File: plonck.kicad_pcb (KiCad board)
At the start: 2 copper layers, 228.6 x 76.2 mm, 127 parts, among them J1 Battery_connector, J2 SWD, J3 Reset, Q1 Q_PMOS_DSG, U1 SRV05-4, U2 TP4054-42-SOT25-R, U3 XC6206PxxxMR-Regulator_Linear, U4 nRF52840_holyiot_18010, q1 USB4085-GF-A_REVA

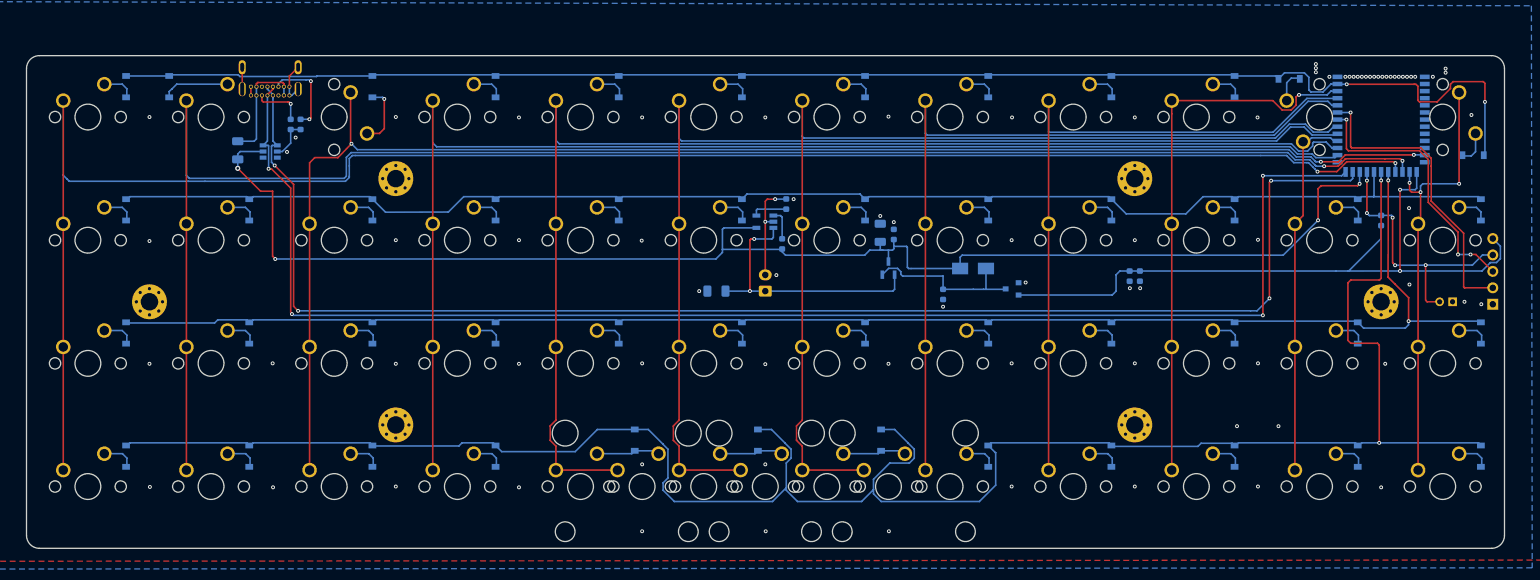
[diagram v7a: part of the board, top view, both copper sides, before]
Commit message: various fixes and additions
changed switch footprints to be alps compatible
added descriptive text to bottom row
fixed mounting holes not being connected to ground
fixed incorrectly wired esd chip
added reset switch in default planck position
changed mx3 to normal rotation
changed board outline to move usb port further out
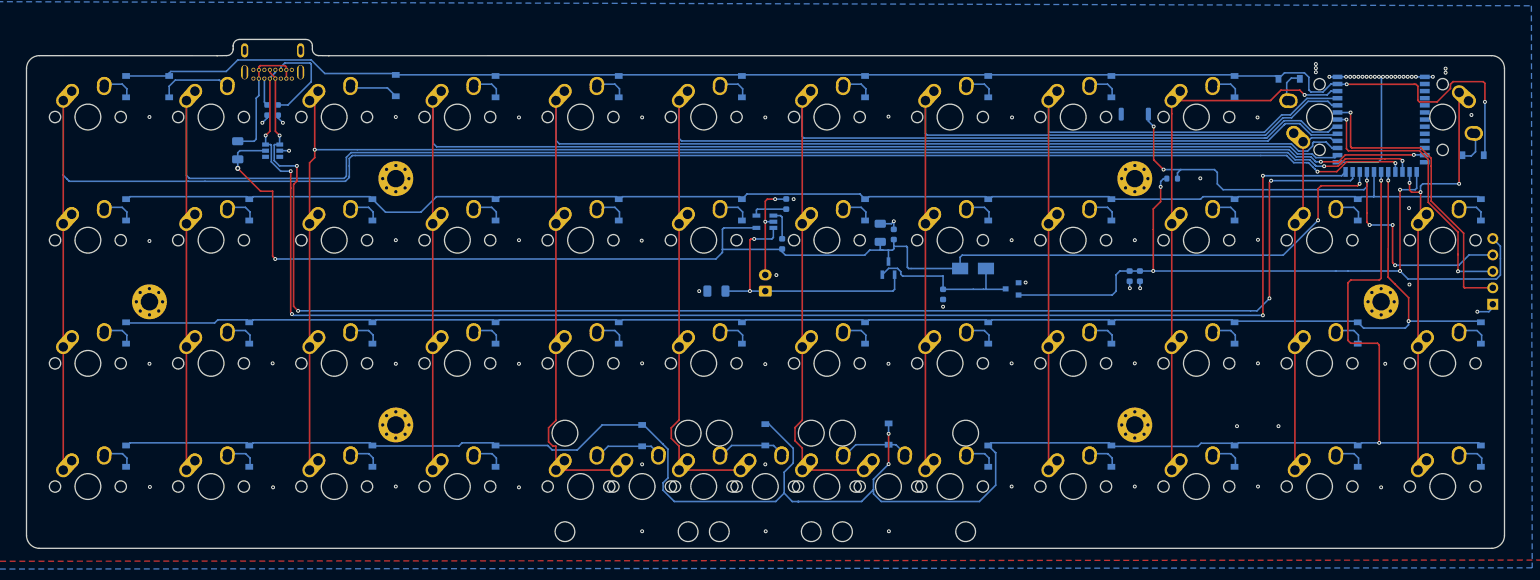
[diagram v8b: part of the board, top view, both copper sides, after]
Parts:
- removed J3: Reset, Connector_PinHeader_2.00mm:PinHeader_1x02_P2.00mm_Vertical
- added SW1: SW_Push, Button_Switch_SMD:SW_Push_SPST_NO_Alps_SKRK, B.Cu at (203.2, 32.9)
- MX1, MX10, MX11, MX12, MX13, MX14, MX15, MX16, MX17, MX18, MX19, MX2, MX20, MX21, MX22, MX23, MX24, MX25, MX26, MX27, MX28, MX29, MX3, MX30, MX31, MX32, MX33, MX34, MX35, MX36, MX37, MX38, MX39, MX4, MX40, MX41, MX42, MX43, MX44, MX45, MX46, MX47, MX48, MX5, MX6, MX7, MX8, MX9: footprint MX_Only:MXOnly-1U-NoLED -> MX_Alps_Hybrid:MX-1U-NoLED
- MX49, MX50, MX51: footprint MX_Only:MXOnly-2U-ReversedStabilizers-NoLED -> MX_Alps_Hybrid:MX-2U-ReversedStabilizers-NoLED
- moved R6 33.0 mm to (209.0, 42.9), turned to 180 degrees
- moved R2 4.25 mm to (69.0, 32.3)
- moved R1 4.14 mm to (70.7, 32.3)
- moved D3 3.62 mm to (88.9, 28.5)
- moved q1 2.63 mm to (69.8, 23.4)
- moved D43 1.50 mm to (165.1, 82.4)
- moved D42 1.41 mm to (146.1, 82.5)
- moved D41 1.34 mm to (127.0, 82.6)
- moved U1 0.40 mm to (69.8, 38.5), turned to 180 degrees
- turned MX3 to 0 degrees
- renumbered J2 to DEBUG
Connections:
- H1 pad 1: (no net) -> GND
- H2 pad 1: (no net) -> GND
- H3 pad 1: (no net) -> GND
- H4 pad 1: (no net) -> GND
- H5 pad 1: (no net) -> GND
- H6 pad 1: (no net) -> GND
- U1 pad 1: Net-(U1-Pad1) -> D-
- U1 pad 2: VBUS -> GND
- U1 pad 3: D+ -> Net-(U1-Pad3)
- U1 pad 4: D- -> Net-(U1-Pad4)
- U1 pad 5: GND -> VBUS
- U1 pad 6: Net-(U1-Pad6) -> D+
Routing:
- net RESET: track 41.8 -> 80.2 mm, vias 5 -> 6
- net GND: track 33.7 -> 54.4 mm, vias 85 -> 84
- net +3V3: track 108.9 -> 117.7 mm, vias 2 -> 4
- net Row4: track 317.0 -> 311.5 mm, vias 2 -> 4
- net D-: track 220.9 -> 225.3 mm, vias 4 -> 5
- net Net-(R2-Pad2): track 7.86 -> 4.26 mm, vias 1 -> 0
- net D+: track 223.7 -> 226.8 mm, vias 4 -> 5
- net Net-(F1-Pad2): track 17.8 -> 20.6 mm
- net Net-(D3-Pad2): track 9.51 -> 7.56 mm, vias 1 -> 0
- net Row1: track 230.3 -> 232.3 mm
- net Row2: track 221.1 -> 219.3 mm
- net 2x2u_2: track 9.89 -> 11.6 mm
- net Net-(R1-Pad2): track 13.2 -> 14.8 mm, vias 2 -> 0
- net 1x2u: track 9.89 -> 11.5 mm
- net SWCLK: track 42.3 -> 43.8 mm, vias 3 -> 2
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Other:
- board size 228.6 x 76.2 mm -> 228.6 x 78.7 mm
- board text added: "+3.3v"
- board text added: "2x2U"
- board text added: "GND"
- board text added: "Grid"
- board text added: "MIT"
- board text added: "RESET"
- board text added: "SWCLK"
- board text added: "SWDIO"
- board text removed: "Reset"
